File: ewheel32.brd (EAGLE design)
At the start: 160 x 30.5 mm, 201 parts, among them Q1 32.768kHz, Q2 8MHz, U1 MK22DX256VLF5, U10 MC74HC595ADTR2G, U11 MC74HC595ADTR2G, U12 MC74HC595ADTR2G, U13 MC74HC595ADTR2G, U14 MC74HC595ADTR2G, U15 MC74HC595ADTR2G, U16 MC74HC595ADTR2G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

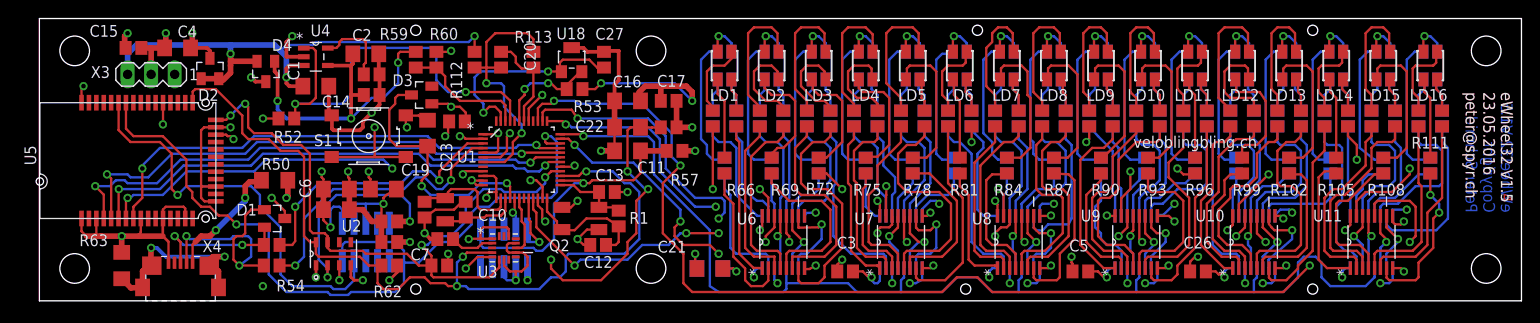
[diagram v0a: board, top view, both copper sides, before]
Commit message: State RGB LED. Second Hall Sensor (ultra low power to wake up from deep sleep). Breakable PCB (MCU part / LED part). Pin head for I2C and SPI.
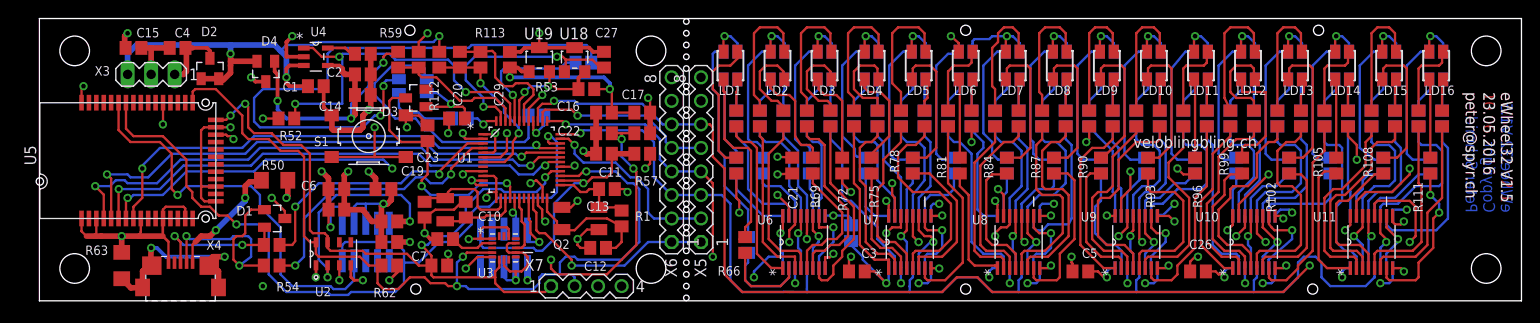
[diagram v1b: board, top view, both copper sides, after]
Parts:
- added C29: 100n, resistor:C0805
- added LD33: CLV1A-FKB, freescale-uc:RGBLED-PLCC4
- added R114, R115, R58: 220, resistor:R0805
- added U19: A3213LH, allegro:SOT23-W
- added X5, X6: (no value), con-lstb:MA08-1
- added X7: (no value), con-lstb:MA04-1
- C1, C11, C16, C18, C19, C2, C21, C22, C23, C25, C4, C6: device resistor:C1206 -> resistor:C0805
- moved C18 15.7 mm to (87.6, 7.30), turned to 90 degrees
- moved C21 14.2 mm to (81.3, 14.6), turned to 270 degrees
- moved R2 8.94 mm to (76.5, 6.03)
- moved R66 8.86 mm to (76.2, 6.03)
- moved R113 5.72 mm to (47.6, 26.0), turned to 270 degrees
- moved R3 5.68 mm to (75.2, 14.6)
- moved R64 5.68 mm to (75.2, 14.6)
- moved C20 4.44 mm to (45.4, 26.0)
- moved R69 4.44 mm to (83.5, 14.6)
- moved R112 3.81 mm to (43.2, 26.0)
- moved R57 3.51 mm to (65.1, 15.9)
- moved C17 3.13 mm to (65.1, 20.3)
- moved C24 2.93 mm to (65.1, 18.1)
- moved C16 2.84 mm to (61.0, 20.3)
- moved C22 2.62 mm to (61.0, 18.1)
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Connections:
- new net LED-B: R115.1, U1.48
- new net LED-G: R114.1, U1.44
- new net LED-R: R58.1, U1.40
- new net N$6: LD33.4, R114.2
- new net N$7: LD33.1, R58.2
- new net N$8: LD33.3, R115.2
- net +3V3: now also C29.1, LD33.2, U19.1, X7.3
- net GND: now also C29.2, U19.3, X5.8, X6.8, X7.4
- net HALL-SENSOR: now also U19.2
- net I2C-SCL: now also X7.2
- net I2C-SDA: now also X7.1
- net SPI-CK: now also X5.5, X6.5
- net SPI-OE: now also X5.1, X6.1
- net SPI-OUT: now also X5.6, X6.6
- net SPI-R: now also X5.4, X6.4
- net SPI-STB: now also X5.3, X6.3
- net SPI-STT: now also X5.2, X6.2
- net V+: now also X5.7, X6.7
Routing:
- net N$6: track 0.00 -> 64.7 mm, vias 0 -> 2
- net N$7: track 0.00 -> 30.5 mm
- net GND: track 202.0 -> 217.2 mm
- net LED-G: track 0.00 -> 14.4 mm, vias 0 -> 1
- net V+: track 127.9 -> 141.5 mm, vias 32 -> 31
- net N$69: track 8.76 -> 20.1 mm
- net VACCU: track 28.5 -> 19.2 mm
- net N$10: track 14.8 -> 22.6 mm
- net N$8: track 0.00 -> 7.78 mm
- net I2C-SDA: track 71.0 -> 78.7 mm
- net D1-B: track 16.8 -> 9.35 mm
- net N$68: track 8.47 -> 15.0 mm
- net D3-G: track 26.8 -> 20.9 mm
- net CHR-STAT: track 45.3 -> 39.8 mm, vias 2 -> 3
- net N$3: track 3.58 -> 9.00 mm
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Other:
- board text added: "10.06.2016"
- board text added: "eWheel32 V2.1"
- board text removed: "eWheel32 V1.4"

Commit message: New Bluetooth Low Energy module BL652
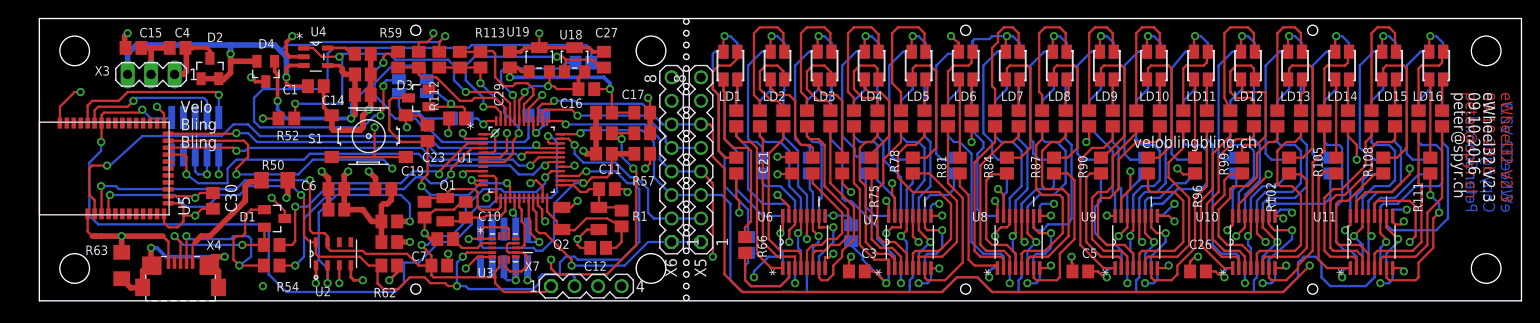
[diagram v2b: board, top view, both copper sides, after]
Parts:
- added C30: 100n, resistor:C0805
- C11: value 1u -> 100n
- U19: value A3213LH -> A3214LH
- U5: value BL600 -> BL652; device ewheel32:BL600 -> ewheel32:BL652
- moved X2 21.7 mm to (16.8, 17.8), turned to 90 degrees
- moved U5 13.2 mm to (7.01, 14.3)
- moved D3 0.32 mm to (41.0, 21.9)
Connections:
- new net BL-SWD-IO: U5.5, X2.P$2
- net +3V3: now also C30.1, U5.26; no longer U5.10
- net BL-LINK: now also U5.38; no longer U5.36
- net BL-RESET: now also U5.7, X2.P$10; no longer U5.22, X2.P$2
- net BL-SWD-CLK: now also U5.6; no longer U5.23
- net GND: now also C30.2, U5.16, U5.27, U5.39; no longer U5.11, U5.17, U5.29, U5.3, U5.31, U5.37, U5.40, U5.43
- net I2C-SCL: now also U5.36; no longer U5.13
- net I2C-SDA: now also U5.37; no longer U5.12
- net UART-CTS-M: now also U5.20; no longer U5.34
- net UART-RTS-M: now also U5.18; no longer U5.35
- net UART-RX: now also U5.19; no longer U5.32
- net UART-TX: now also U5.17; no longer U5.33
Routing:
- net BL-SWD-CLK: track 44.7 -> 16.0 mm
- net BL-SWD-IO: track 0.00 -> 19.2 mm, vias 0 -> 1
- net GND: track 217.2 -> 203.3 mm
- net UART-RX: track 57.2 -> 43.8 mm
- net UART-TX: track 56.4 -> 43.6 mm
- net I2C-SDA: track 78.7 -> 87.5 mm
- net BL-LINK: track 53.4 -> 59.2 mm
- net UART-CTS-M: track 53.9 -> 48.4 mm
- net BL-RESET: track 87.2 -> 91.7 mm, vias 2 -> 3
- net SPI-OE: track 151.0 -> 147.8 mm
- net I2C-SCL: track 96.5 -> 99.6 mm, vias 3 -> 5
- net UART-RTS-M: track 57.9 -> 55.4 mm
- net +3V3: track 78.7 -> 76.5 mm
- net N$59: track 23.0 -> 24.2 mm
- net SPI-STT: track 134.6 -> 135.7 mm
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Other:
- board text added: "09.10.2016"
- board text added: "Bling"
- board text added: "Velo"
- board text added: "eWheel32 V2.3"
- board text removed: "10.06.2016"
- board text removed: "23.05.2016"
- board text removed: "eWheel32 V1.5"
- board text removed: "eWheel32 V2.1"
